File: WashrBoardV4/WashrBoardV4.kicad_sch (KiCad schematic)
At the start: 37 parts, among them J1 TestPoint 5V, J10 ProgPoint GND, J2 USB_C_Receptacle_USB2.0_16P, J3 TestPoint GND, J4 TestPoint 3.3V, J5 JST GH, J6 ProgPoint 5V, J7 ProgPoint P9 GND, J8 ProgPointPoint D_P, J9 ProgPoint D_N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

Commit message: Initial PCB layout w/out traces
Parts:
- J1, J10, J3, J4, J6, J7, J8, J9: footprint TestPoint:TestPoint_Pad_D2.0mm -> TestPoint:TestPoint_Pad_D1.0mm
- J5: footprint Connector_JST:JST_GH_SM02B-GHS-TB_1x02-1MP_P1.25mm_Horizontal -> Connector_JST:JST_XH_S2B-XH-A-1_1x02_P2.50mm_Horizontal
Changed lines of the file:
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@@
 			)
 		)
-		(property "Footprint" "TestPoint:TestPoint_Pad_D2.0mm"
+		(property "Footprint" "TestPoint:TestPoint_Pad_D1.0mm"
 			(at 238.76 135.89 0)
 			(effects
@@
 			)
 		)
-		(property "Footprint" "TestPoint:TestPoint_Pad_D2.0mm"
+		(property "Footprint" "TestPoint:TestPoint_Pad_D1.0mm"
 			(at 218.44 125.73 0)
 			(effects
@@
 			)
 		)
-		(property "Footprint" "TestPoint:TestPoint_Pad_D2.0mm"
+		(property "Footprint" "TestPoint:TestPoint_Pad_D1.0mm"
 			(at 218.44 147.32 0)
 			(effects
@@
 			)
 		)
-		(property "Footprint" "TestPoint:TestPoint_Pad_D2.0mm"
+		(property "Footprint" "TestPoint:TestPoint_Pad_D1.0mm"
 			(at 218.44 157.48 0)
 			(effects
@@
 			)
 		)
-		(property "Footprint" "TestPoint:TestPoint_Pad_D2.0mm"
+		(property "Footprint" "TestPoint:TestPoint_Pad_D1.0mm"
 			(at 48.26 71.12 0)
 			(effects
@@
 			)
 		)
-		(property "Footprint" "TestPoint:TestPoint_Pad_D2.0mm"
+		(property "Footprint" "TestPoint:TestPoint_Pad_D1.0mm"
 			(at 31.75 60.96 0)
 			(effects
@@
 			)
 		)
-		(property "Footprint" "TestPoint:TestPoint_Pad_D2.0mm"
+		(property "Footprint" "TestPoint:TestPoint_Pad_D1.0mm"
 			(at 218.44 135.89 0)
 			(effects
@@
 			)
 		)
-		(property "Footprint" "TestPoint:TestPoint_Pad_D2.0mm"
+		(property "Footprint" "TestPoint:TestPoint_Pad_D1.0mm"
 			(at 59.69 60.96 0)
 			(effects
@@
 			)
 		)
-		(property "Footprint" "Connector_JST:JST_GH_SM02B-GHS-TB_1x02-1MP_P1.25mm_Horizontal"
+		(property "Footprint" "Connector_JST:JST_XH_S2B-XH-A-1_1x02_P2.50mm_Horizontal"
 			(at 123.19 115.57 0)
 			(effects
@@
 			)
 		)
-		(property "Datasheet" "https://www.digikey.com/en/products/detail/jst-sales-america-inc/SM02B-GHS-TB/807786"
+		(property "Datasheet" "https://www.digikey.com/en/products/detail/jst-sales-america-inc/S2B-XH-A-1/9961922"
 			(at 123.19 115.57 0)
 			(effects

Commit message: Prepared schematic for BOM export
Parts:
- C1, C2, C6: Manufacturer Part Number (none) -> CL31B105KCHNNNE
- C3: Manufacturer Part Number (none) -> 1206B104K500CT
- C4: Manufacturer Part Number (none) -> CC1206KRX7R9BB103
- C5: Manufacturer Part Number (none) -> UMK316BJ225KD-T
- D1: Manufacturer Part Number (none) -> HSMG-C150
- D2: Manufacturer Part Number (none) -> SML-D12U1WT86
- J1, J10, J3, J4, J6, J7, J8, J9: now left out of the parts list
- J2: Manufacturer Part Number (none) -> USB4105-GF-A
- J5: Manufacturer Part Number (none) -> S2B-XH-A-1
- MT1: value ~ -> IMU; Manufacturer Part Number (none) -> ICM-42670-P
- R1, R2: Manufacturer Part Number (none) -> CRCW12065K10FKEA
- R10, R7, R8, R9: Manufacturer Part Number (none) -> RR1220P-103-D
- R3, R5: Manufacturer Part Number (none) -> RT1206FRE074K7L
- R4, R6: Manufacturer Part Number (none) -> CRCW120675R0FKEA
- U1: value ~ -> Regulator; Manufacturer Part Number (none) -> TLV1117LV33DCYR
- U2: Manufacturer Part Number (none) -> USBLC6-2SC6
- U3: Manufacturer Part Number (none) -> PTS526SK15SMTR2 LFS
- U4: Manufacturer Part Number (none) -> ESP32-C3-WROOM-02U-N4

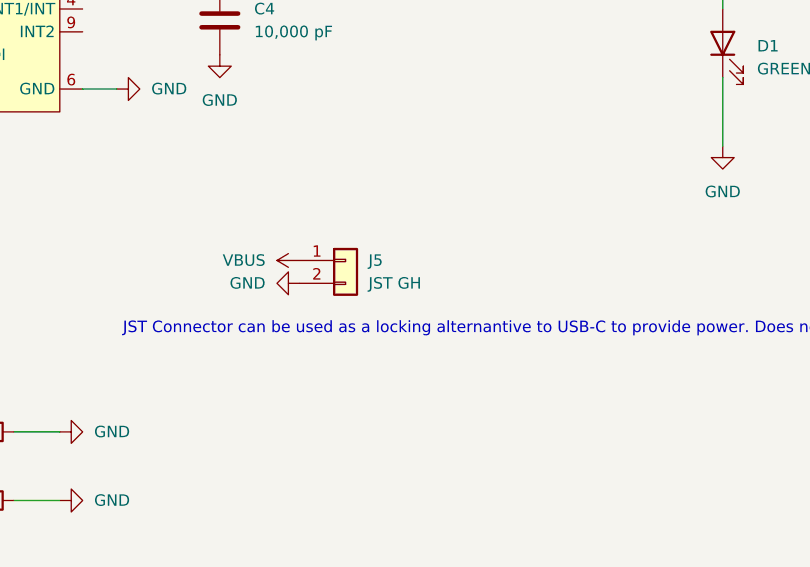
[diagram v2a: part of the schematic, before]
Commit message: Changed label on JST connector
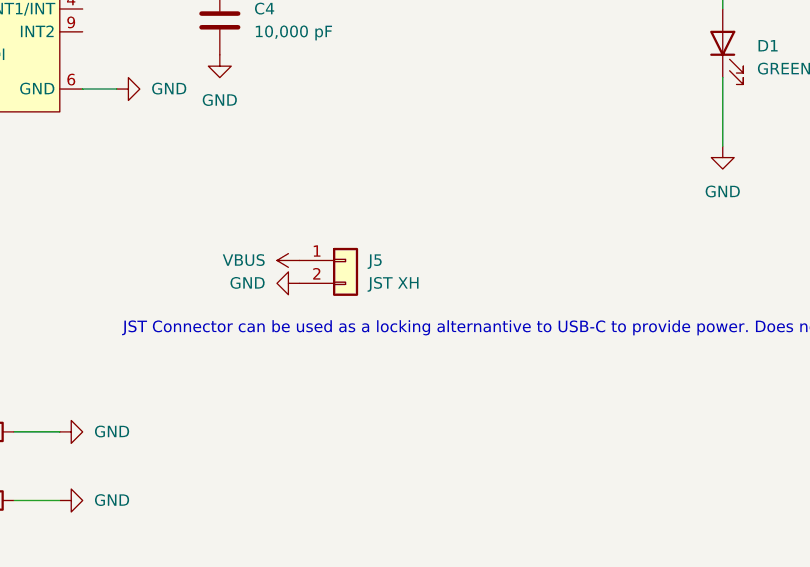
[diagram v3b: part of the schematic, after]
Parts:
- J5: value JST GH -> JST XH
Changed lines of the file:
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@@
 	(label "SDA"
 		(at 54.61 92.71 0)
+		(fields_autoplaced yes)
 		(effects
 			(font
@@
 	(label "D_P"
 		(at 223.52 147.32 0)
+		(fields_autoplaced yes)
 		(effects
 			(font
@@
 	(label "D_P"
 		(at 63.5 151.13 0)
+		(fields_autoplaced yes)
 		(effects
 			(font
@@
 	(label "ProgGND"
 		(at 207.01 109.22 0)
+		(fields_autoplaced yes)
 		(effects
 			(font
@@
 	(label "D_P"
 		(at 92.71 34.29 0)
+		(fields_autoplaced yes)
 		(effects
 			(font
@@
 	(label "D_N"
 		(at 63.5 146.05 0)
+		(fields_autoplaced yes)
 		(effects
 			(font
@@
 	(label "ProgGND"
 		(at 223.52 135.89 0)
+		(fields_autoplaced yes)
 		(effects
 			(font
@@
 	(label "D-"
 		(at 213.36 81.28 0)
+		(fields_autoplaced yes)
 		(effects
 			(font
@@
 	(label "D+"
 		(at 213.36 83.82 0)
+		(fields_autoplaced yes)
 		(effects
 			(font
@@
 	(label "D_N"
 		(at 223.52 157.48 0)
+		(fields_autoplaced yes)
 		(effects
 			(font
@@
 	(label "D-"
 		(at 110.49 31.75 0)
+		(fields_autoplaced yes)
 		(effects
 			(font
@@
 	(label "SCL"
 		(at 54.61 90.17 0)
+		(fields_autoplaced yes)
 		(effects
 			(font
@@
 	(label "D_N"
 		(at 92.71 31.75 0)
+		(fields_autoplaced yes)
 		(effects
 			(font
@@
 	(label "SCL"
 		(at 177.8 66.04 0)
+		(fields_autoplaced yes)
 		(effects
 			(font
@@
 	(label "D+"
 		(at 110.49 34.29 0)
+		(fields_autoplaced yes)
 		(effects
 			(font
@@
 	(label "SDA"
 		(at 177.8 63.5 0)
+		(fields_autoplaced yes)
 		(effects
 			(font
@@
 			)
 		)
-		(property "Value" "JST GH"
+		(property "Value" "JST XH"
 			(at 125.73 118.1099 0)
 			(effects
